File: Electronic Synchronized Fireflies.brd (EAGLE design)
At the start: 37 x 35 mm, 30 parts, among them Q1 BSS123, Q2 BSS84, Q3 LPT80A, Q4 LPT80A, Q5 LPT80A, U1 NCP1400A, U2 MSP430G2231

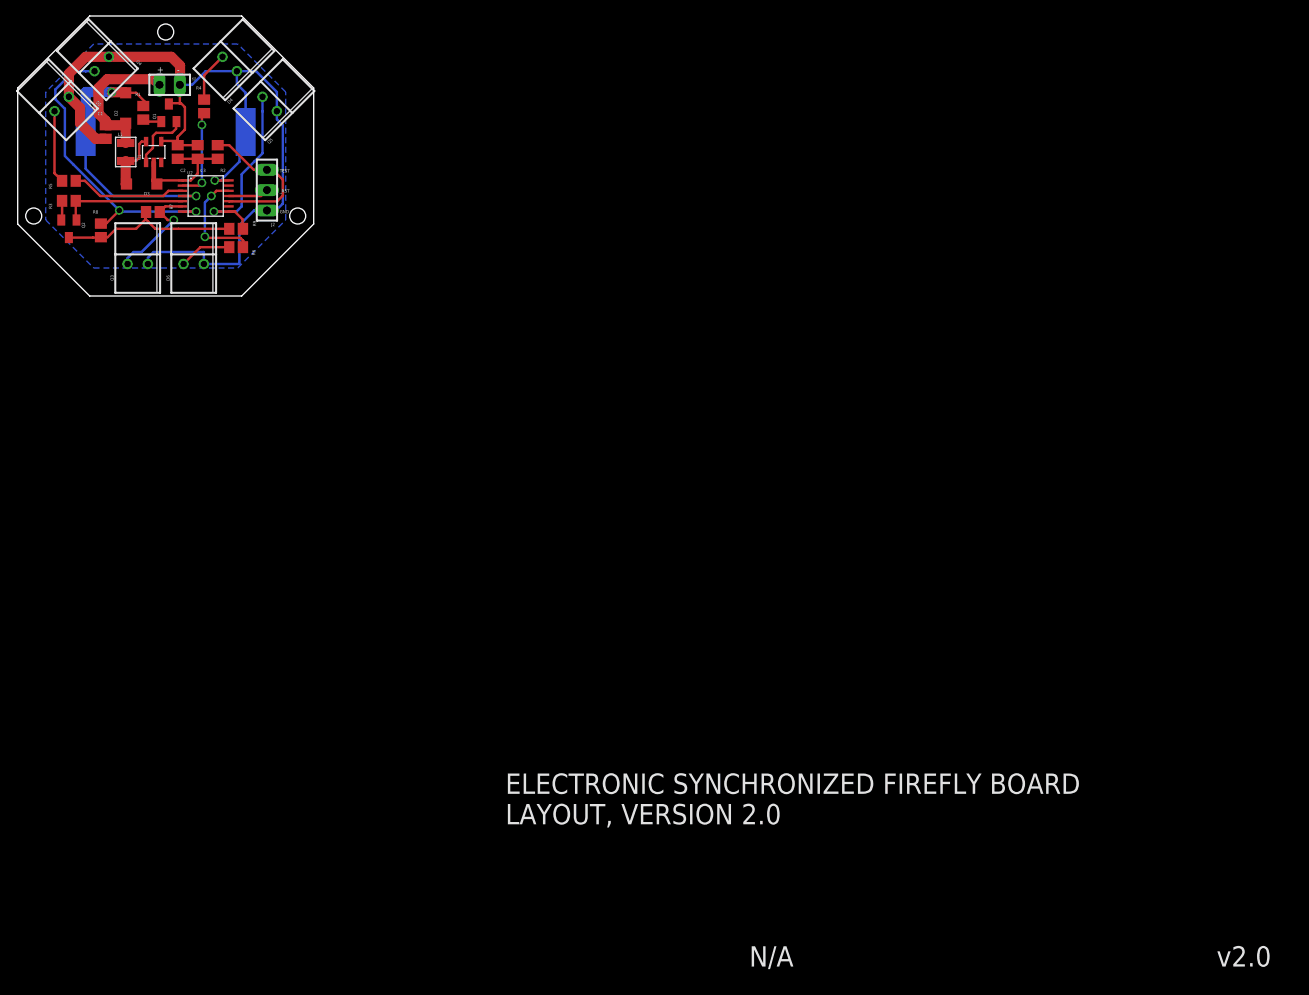
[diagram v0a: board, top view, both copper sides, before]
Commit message: Move back to LDR setup
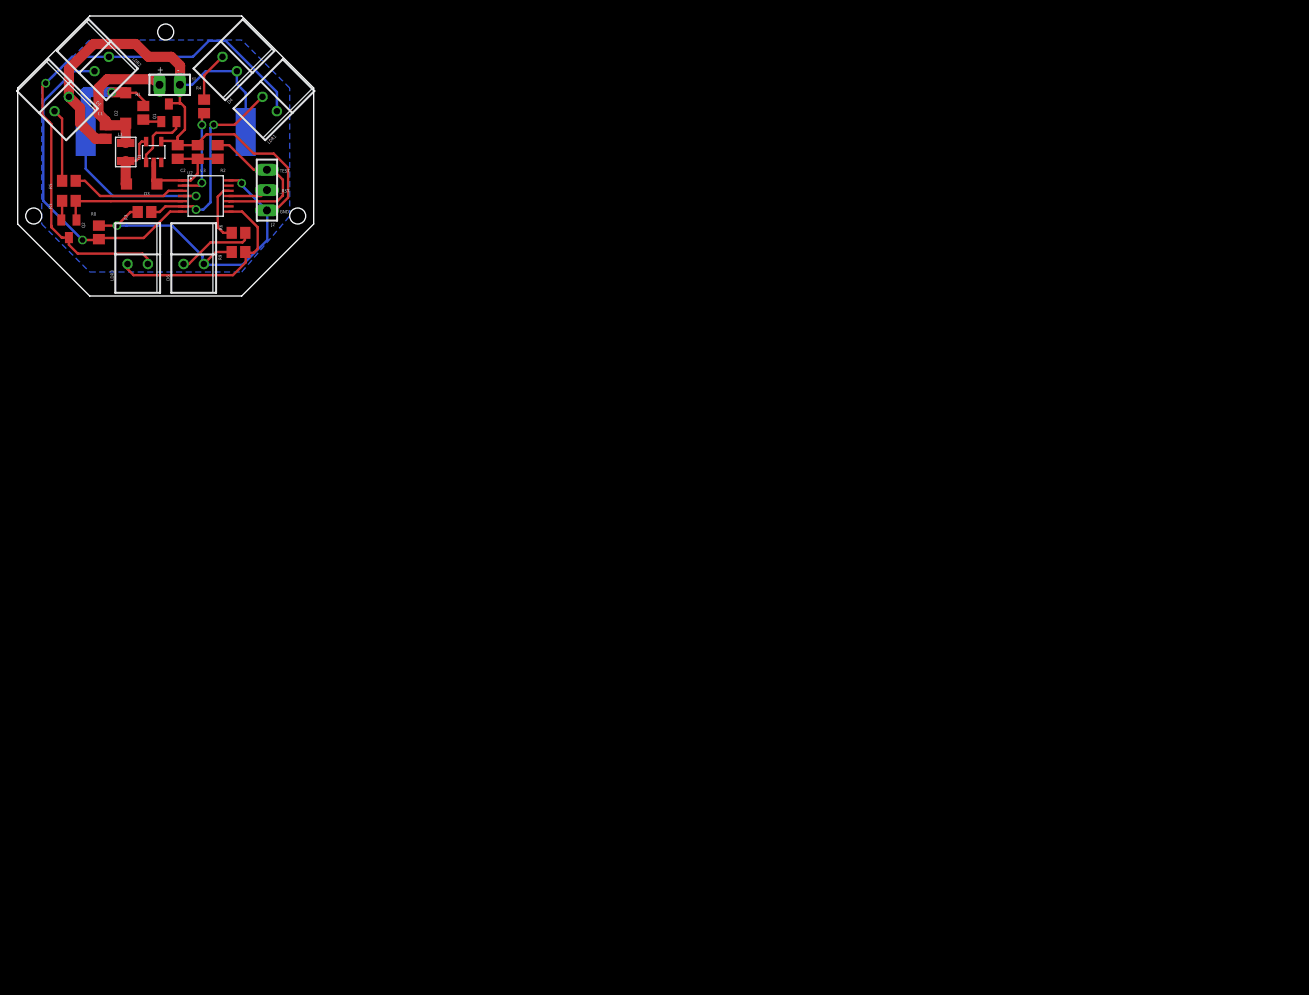
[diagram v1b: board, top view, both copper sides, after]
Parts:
- LDR1, LDR2, LDR3: value LPT80A -> LDRRTANGLEHOLDER
- moved R9 2.92 mm to (27.6, 5.50), turned to 0 degrees
- moved R6 1.82 mm to (27.6, 7.90), turned to 180 degrees
- moved R7 1.05 mm to (15.8, 10.5), turned to 0 degrees
- moved R8 0.35 mm to (10.2, 7.95)
- renumbered Q3 to LDR3, Q4 to LDR2, Q5 to LDR1
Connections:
- removed net N$14: LDR3.A, R7.1, U2.6
- new net N$8: LDR1.A, R7.2, U2.6
- net GND: now also R7.1, R8.1, R9.1; no longer LDR1.K, LDR2.K, LDR3.K
- net N$12: now also LDR1.K, LDR2.K, LDR3.K; no longer R7.2, R8.2, R9.2
- net N$13: now also R8.2; no longer R8.1
- net N$15: now also LDR3.A, R9.2; no longer LDR1.A, R9.1
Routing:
- net N$12: track 22.4 -> 69.6 mm, vias 0 -> 1
- net N$8: track 0.00 -> 25.6 mm, vias 0 -> 2
- net N$14: track 13.8 -> 0.00 mm, vias 1 -> 0
- net GND: track 116.1 -> 124.7 mm, vias 1 -> 2
- net N$18: track 13.7 -> 7.55 mm, vias 2 -> 0
- net N$21: track 6.59 -> 9.83 mm
- net N$13: track 39.0 -> 41.3 mm, vias 2 -> 1
- net N$15: track 24.5 -> 26.6 mm, vias 1 -> 0
